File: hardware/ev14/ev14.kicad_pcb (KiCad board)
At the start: 4 copper layers, 75.2 x 80 mm, 173 parts, among them CN1 Conn_05x02_Female, J1 USB_C_Receptacle, J10 Conn_02x05_Counter_Clockwise, J2 Conn_01x02_Socket, J3 AudioJack4, J4 AudioJack4, J5 Conn_02x03_Odd_Even, J6 Conn_01x35_Socket, J7 Conn_02x05_Counter_Clockwise, J8 Conn_02x05_Counter_Clockwise, J9 Conn_02x05_Counter_Clockwise, Q1 2N7002, Q2 Q_Dual_NMOS_S1G1D2S2G2D1, Q3 PMOS, SW1 SW_SPDT, SW2 SW_Push, SW3 SW_Push, SW4 SW_Push, SW5 SW_Push, U1 BQ21040DBV, U10 STM32F405RGTx, U2 USBLC6-2P6, U3 STM32F072CBTx, U4 CH340C, U5 TPS63060, U6 WM8960CGEFL/RV, U7 ESP32-S3-WROOM-1, U8 M24C02-RMN6TP, U9 BM14B(0.8)-24DS-0.4V(53), Y1 Crystal_GND24

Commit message: First finished draft of Ev14
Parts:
- removed TP1, TP2, TP3, TP4: TestPoint, TestPoint:TestPoint_THTPad_D2.0mm_Drill1.0mm
- moved J10 3.19 mm to (233.2, 125.3)
- moved J7 3.19 mm to (246.8, 125.4)
- moved J8 3.19 mm to (233.2, 109.3)
- moved J9 3.19 mm to (246.9, 109.4)
- moved U2 1.95 mm to (197.9, 122.5), turned to 90 degrees
- moved C46 1.91 mm to (196.8, 119.1)
- moved R61 1.91 mm to (197.8, 119.1)
- moved R57 0.88 mm to (195.8, 119.2)
- moved SW3 0.08 mm to (176.5, 100.8)
- moved SW2 0.08 mm to (176.5, 109.6)
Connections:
- U10 pad 16: /UI_TX2_NET -> /UI_TX2_NET_N
- U10 pad 17: /UI_RX2_NET -> /UI_RX2_NET_P
- U7 pad 10: /UI_RX2_NET_- -> /UI_RX2_NET_P
- U7 pad 11: /UI_TX2_NET_+ -> /UI_TX2_NET_N
- U9 pad 23: /KB_LEDK_2&3 -> unconnected-(U9-Pad23)
- U9 pad 24: /KB_LEDA_3&4 -> unconnected-(U9-Pad24)
- U9 pad 25: /KB_LEDK_1&4 -> unconnected-(U9-Pad25)
- U9 pad 26: /KB_LEDA_1&2 -> unconnected-(U9-Pad26)
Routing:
- net +3.3V: track 134.3 -> 189.8 mm, vias 33 -> 41
- net GNDA: track 98.1 -> 152.5 mm, vias 7 -> 8
- net GND: track 232.4 -> 279.7 mm, vias 95 -> 109
- net /UI_TX2_NET: track 101.0 -> 126.9 mm, vias 2 -> 4
- net /UI_RX2_NET: track 101.0 -> 126.4 mm, vias 2 -> 4
- net /MGMT_NRST: track 97.5 -> 119.4 mm
- net /MGMT_BOOT: track 102.2 -> 122.4 mm
- net VBUS: track 27.1 -> 33.8 mm, vias 2 -> 4
- net /D_P: track 4.24 -> 10.5 mm
- net /D_N: track 6.08 -> 10.4 mm
- net /UI_SDA: track 141.3 -> 145.5 mm
- net /NET_TX1_MGMT: track 73.1 -> 77.1 mm
- net /UI_RTS1_MGMT: track 119.9 -> 123.6 mm
- net /USB_TX1_MGMT: track 54.7 -> 58.4 mm
- net /NET_RX1_MGMT: track 71.3 -> 74.7 mm
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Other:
- board size 75.2 x 80 mm -> 78.4 x 80 mm
- board text added: "EV14"
- board text added: "Finn Berg 2025/07/17"

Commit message: Updated complete EV14 draft
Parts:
- added J11: Conn_02x05_Counter_Clockwise, Hactar_Footprints:HDR-SMD_10P-P2.54-V-F-R2-C5-LS7.1-1, F.Cu at (245.7, 117.4)
- moved J7 12.2 mm to (258.9, 125.3)
- moved J9 12.0 mm to (258.9, 109.3)
- moved R65 0.41 mm to (215.1, 54.5)
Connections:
- U10 pad 16: /UI_TX2_NET_N -> /UI_TX2_NET
- U10 pad 17: /UI_RX2_NET_P -> /UI_RX2_NET
- U10 pad 20: /UI_LED_R -> /MIC_IO
- U10 pad 53: /MIC_IO -> /UI_LED_R
- U7 pad 10: /UI_RX2_NET_P -> /UI_RX2_NET
- U7 pad 11: /UI_TX2_NET_N -> /UI_TX2_NET
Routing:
- net GND: track 279.7 -> 342.6 mm, vias 109 -> 111
- net /UI_RX2_NET: track 126.4 -> 175.9 mm, vias 4 -> 5
- net /UI_TX2_NET: track 126.9 -> 175.4 mm, vias 4 -> 5
- net +3.3V: track 189.8 -> 221.3 mm, vias 41 -> 43
- net /NET_TX1_MGMT: track 77.1 -> 105.9 mm
- net /NET_RX1_MGMT: track 74.7 -> 102.4 mm
- net GNDA: track 152.5 -> 177.8 mm
- net /UI_RTS1_MGMT: track 123.6 -> 140.6 mm, vias 5 -> 3
- net Net-(J9-Pin_6): track 64.8 -> 81.7 mm
- net /MGMT_BOOT: track 122.4 -> 107.3 mm
- net Net-(J9-Pin_7): track 69.6 -> 84.6 mm
- net /MGMT_NRST: track 119.4 -> 104.7 mm
- net Net-(J9-Pin_8): track 72.9 -> 87.4 mm
- net /UI_CTS1_MGMT: track 119.6 -> 133.3 mm, vias 5 -> 3
- net /USB_RX1_MGMT: track 67.7 -> 81.0 mm
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- removed copper zone on B.Cu, net GNDA
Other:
- board size 78.4 x 80 mm -> 94.4 x 80 mm
- board text added: "+3.3V"
- board text added: "+3.3V -->"
- board text added: "BATTERY"
- board text added: "BOOT0"
- board text added: "DISPLAY"
- board text added: "FINN BERG 2025/07/22"
- board text added: "GND"
- board text added: "GND -->"
- board text added: "I2S_ADCDAT"
- board text added: "I2S_BCLK"
- board text added: "I2S_DACDAT"
- board text added: "I2S_DACLRC"
- board text added: "KEYBOARD"
- board text added: "LED_A"
- board text added: "LED_B"
- board text added: "LED_NET"
- board text added: "LED_UI"
- board text added: "MCLK"
- board text added: "MGMT_BOOT"
- board text added: "MGMT_CPU"
- board text added: "MGMT_DEBUG_1"
- board text added: "MGMT_DEBUG_2"
- board text added: "MGMT_NRST"
- board text added: "MGMT_SWCLK"
- board text added: "MGMT_SWDIO"
- board text added: "NET J-tag"
- board text added: "NET_BOOT"
- board text added: "NET_CPU"
- board text added: "NET_DEBUG_1"
- board text added: "NET_DEBUG_2"
- board text added: "NET_DEBUG_3"
- board text added: "NET_NRST"
- board text added: "NET_RX1_MGMT"
- board text added: "NET_TX1_MGMT"
- board text added: "NRST"
- board text added: "OSCILLATOR"
- board text added: "P2T"
- board text added: "P2T2AI"
- board text added: "Pin out: 1:3.3V 2:NET_MTMS 3:GND 4:NET_MTCK 5:GND 6:NET_MTDO 7:GND 8:NET_MTDI 9:GND 10:X"
- board text added: "SNAP HERE"
- board text added: "SWCLK"
- board text added: "SWDIO"
- board text added: "UI ST-Link"
- board text added: "UI_CPU"
- board text added: "UI_CTS1_MGMT"
- board text added: "UI_DEBUG_1"
- board text added: "UI_DEBUG_2"
- board text added: "UI_RTS1_MGMT"
- board text added: "UI_RX1_MGMT"
- board text added: "UI_RX2_NET"
- board text added: "UI_SCL"
- board text added: "UI_SDA"
- board text added: "UI_TX1_MGMT"
- board text added: "UI_TX2_NET"
- board text added: "USB_RX1_MGMT"
- board text added: "USB_TX1_MGMT"
- board text added: "VIN"
- board text added: "VOUT"
- board text added: "X"
- board text removed: "Finn Berg 2025/07/17"

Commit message: Final Version of EV14
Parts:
- removed J4: AudioJack4, Hactar_Footprints:AUDIO-SMD_PJ-242
- removed R37: 100k, Resistor_SMD:R_0402_1005Metric
- removed R63: 1k0, Resistor_SMD:R_0402_1005Metric
- added C49: 100n, Capacitor_SMD:C_0402_1005Metric, F.Cu at (191.7, 65.5)
- added CN2: PJ-242, Hactar_Footprints:AUDIO-SMD_PJ-242D-SMT, F.Cu at (189.3, 58.3)
- added R75: 4k7, Resistor_SMD:R_0402_1005Metric, F.Cu at (185.0, 55.6)
- J10: value Conn_02x05_Counter_Clockwise -> Conn_02x04_Odd_Even; footprint Hactar_Footprints:HDR-SMD_10P-P2.54-V-F-R2-C5-LS7.1-1 -> Hactar_Footprints:HDR-SMD_8P-P2.54-V-M-R2-C4-LS7.4
- moved J10 1.57 mm to (233.3, 126.8)
- moved Q3 0.32 mm to (182.6, 55.2)
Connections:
- net /UI_SCL renamed /UI_SCL1
- net /UI_SDA renamed /UI_SDA1
- J10 pad 2: /NET_TX1_MGMT -> /MGMT_SWCLK
- J10 pad 3: /NET_RX1_MGMT -> /NET_TX1_MGMT
- J10 pad 4: /NET_NRST -> /MGMT_SWDIO
- J10 pad 5: GND -> /NET_RX1_MGMT
- J10 pad 6: GND -> /MGMT_NRST
- J10 pad 7: /MGMT_BOOT -> /NET_NRST
- J10 pad 8: /MGMT_NRST -> /MGMT_BOOT
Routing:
- net +3.3V: track 221.3 -> 243.0 mm, vias 43 -> 44
- net Net-(Q2A-G): track 8.91 -> 22.2 mm, vias 0 -> 2
- net GND: track 342.6 -> 335.9 mm, vias 111 -> 110
- net /HP_R: track 25.1 -> 21.9 mm
- net GNDA: track 177.8 -> 180.4 mm, vias 8 -> 9
- net /NET_NRST: track 89.7 -> 92.0 mm
- net /MCLK: track 133.1 -> 131.4 mm
- net /MGMT_SWDIO: track 47.3 -> 45.9 mm
- net /UI_SCL1: track 144.1 -> 142.9 mm
- net /NET_TX1_MGMT: track 105.9 -> 107.0 mm
- net /NET_RX1_MGMT: track 102.4 -> 103.5 mm
- net /UI_RTS2_NET: track 52.2 -> 53.1 mm
- net /MGMT_NRST: track 104.7 -> 103.8 mm
- net Net-(Q2B-D): track 4.13 -> 3.27 mm
- net /UI_TX2_NET: track 175.4 -> 174.6 mm
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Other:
- outline, holes or cut-outs redrawn
- board text added: "BOARD"
- board text added: "CISCO"
- board text added: "DEV"

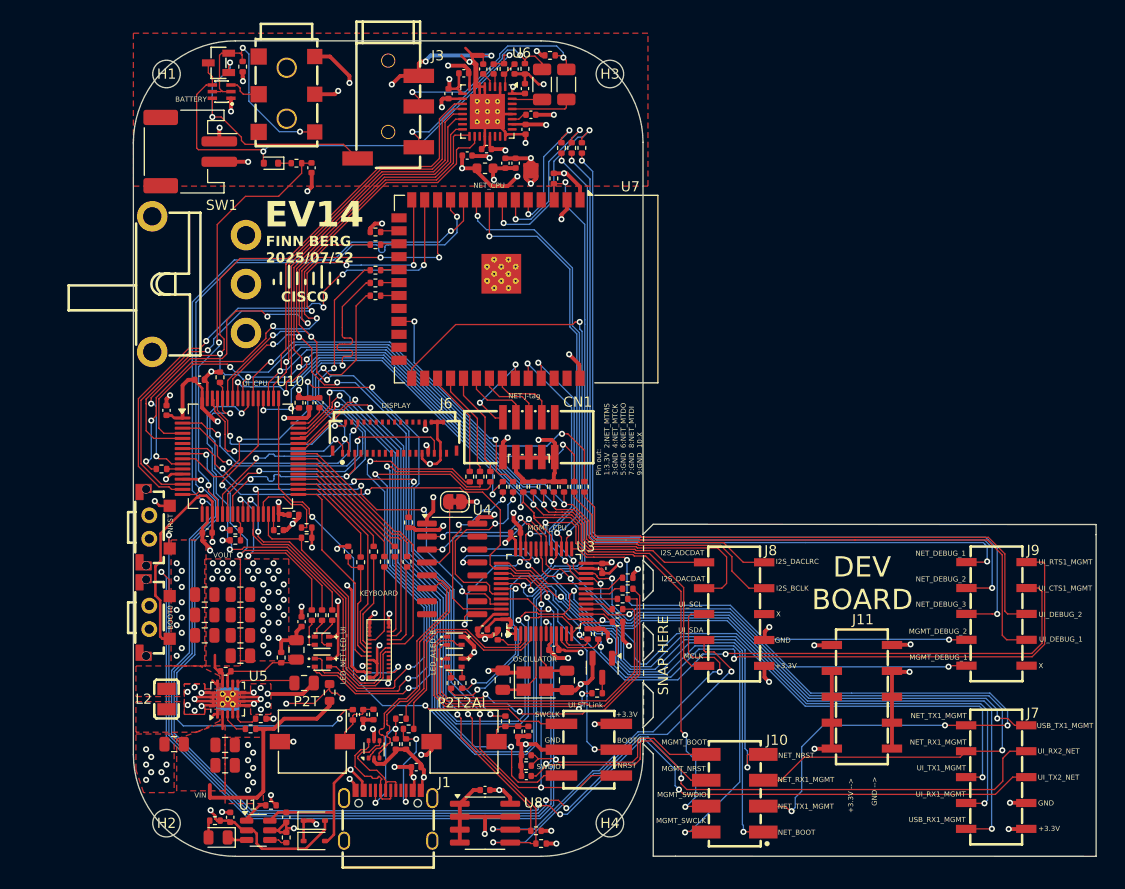
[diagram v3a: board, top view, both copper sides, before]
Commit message: chore: update headphone jacks to be 11.46mm apart. Fix issues that arose from that
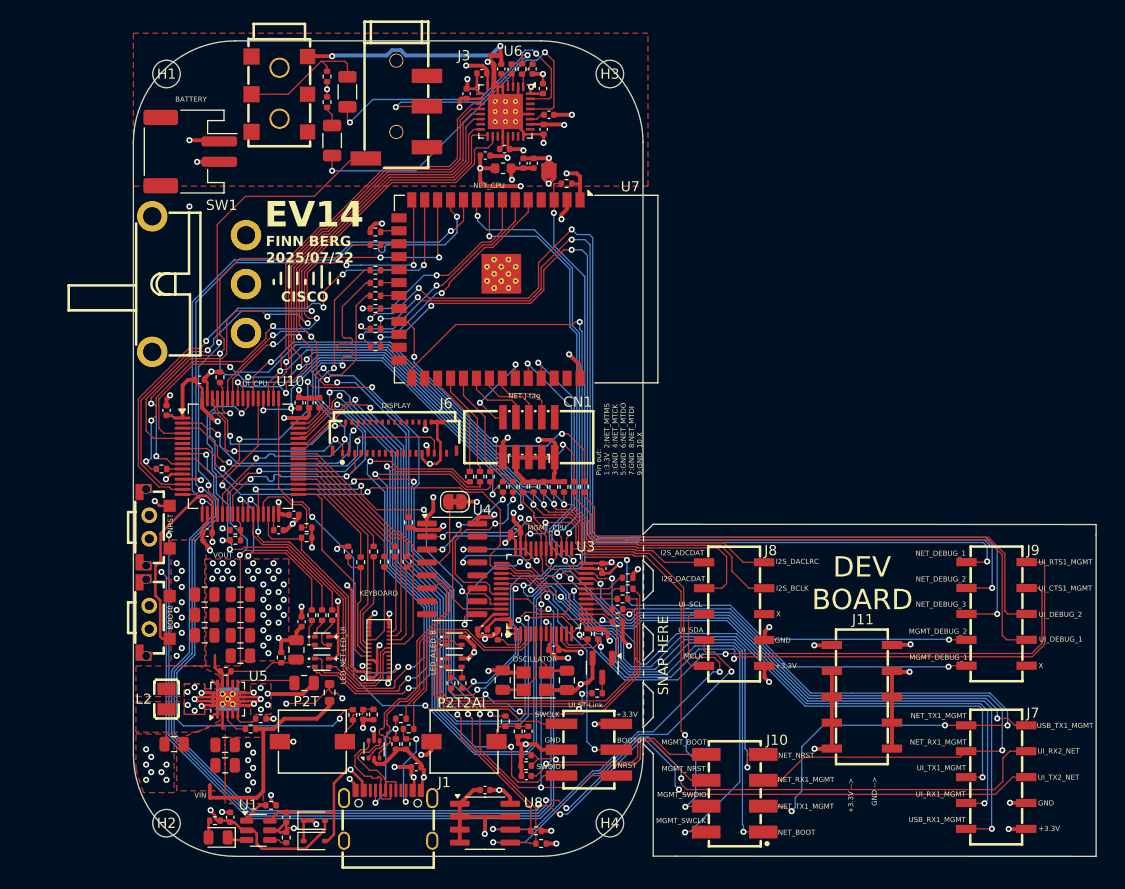
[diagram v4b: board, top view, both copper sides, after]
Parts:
- removed C49: 100n, Capacitor_SMD:C_0402_1005Metric
- removed D7: 1N4148WT, Diode_SMD:D_SOD-523
- removed Q2: Q_Dual_NMOS_S1G1D2S2G2D1, Hactar_Footprints:SOT-363_L2.1-W1.3-P0.65-LS2.3-BL
- removed Q3: PMOS, Hactar_Footprints:SOT-23-3_L2.9-W1.3-P1.90-LS2.4-BR
- removed R36: 47k, Resistor_SMD:R_0402_1005Metric
- removed R75: 4k7, Resistor_SMD:R_0402_1005Metric
- moved R70 26.7 mm to (198.0, 83.0), turned to 0 degrees
- moved R71 26.2 mm to (198.0, 81.3), turned to 0 degrees
- moved R72 25.7 mm to (198.0, 79.3), turned to 0 degrees
- moved C48 23.6 mm to (193.8, 62.8)
- moved R65 22.4 mm to (193.3, 59.0), turned to -90 degrees
- moved R32 19.4 mm to (193.3, 56.5)
- moved C34 19.1 mm to (195.3, 58.0)
- moved C10 1.77 mm to (212.5, 65.0)
- moved C11 1.77 mm to (213.5, 65.0)
- moved C28 1.77 mm to (210.7, 63.7)
- moved C33 1.77 mm to (215.0, 60.3)
- moved C36 1.77 mm to (211.4, 55.8)
- moved C37 1.77 mm to (213.4, 55.8)
- moved C7 1.77 mm to (208.8, 64.3)
- moved JP2 1.77 mm to (209.8, 54.5)
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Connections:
- CN2 pad 4: GNDA -> unconnected-(CN2-Pad4)
- CN2 pad 5: Net-(Q2A-G) -> unconnected-(CN2-Pad5)
- CN2 pad 6: Net-(Q2B-D) -> /HP_L
- J3 pad R1: /HP_R -> /MIC_P
- J3 pad R2: /MIC_N -> unconnected-(J3-PadR2)
- J3 pad S: Net-(Q2A-D) -> /MIC_IO
- J3 pad T: /HP_L -> unconnected-(J3-PadT)
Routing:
- net GNDA: track 180.4 -> 139.5 mm, vias 9 -> 7
- net Net-(U6-HP_R): track 6.16 -> 35.3 mm, vias 0 -> 2
- net /MIC_P: track 47.9 -> 19.7 mm
- net Net-(U6-HP_L): track 3.20 -> 30.4 mm, vias 0 -> 2
- net Net-(Q2A-D): track 25.1 -> 0.00 mm, vias 2 -> 0
- net Net-(Q2A-G): track 22.2 -> 0.00 mm, vias 2 -> 0
- net Net-(J9-Pin_8): track 87.4 -> 108.1 mm, vias 2 -> 4
- net /HP_R: track 21.9 -> 1.99 mm, vias 2 -> 0
- net Net-(J9-Pin_7): track 84.6 -> 101.3 mm, vias 2 -> 4
- net +3.3V: track 243.0 -> 226.7 mm, vias 44 -> 43
- net Net-(J9-Pin_6): track 81.7 -> 96.8 mm, vias 2 -> 4
- net /NET_DEBUG_1: track 13.0 -> 24.2 mm
- net GND: track 335.9 -> 326.6 mm
- net /HP_L: track 20.3 -> 13.1 mm, vias 2 -> 0
- net /NET_DEBUG_2: track 15.7 -> 22.7 mm
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
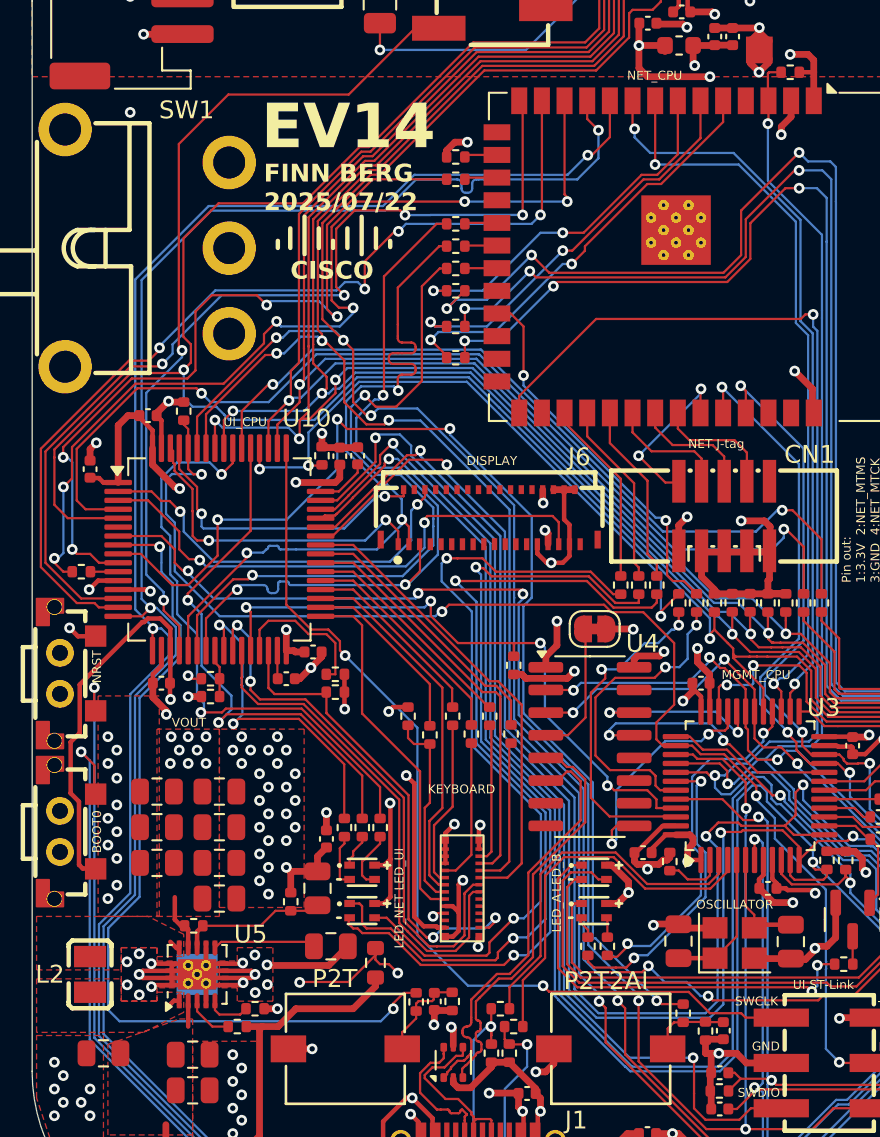
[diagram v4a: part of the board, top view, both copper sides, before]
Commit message: feat: cleaned up remaining pcb errors and warnings
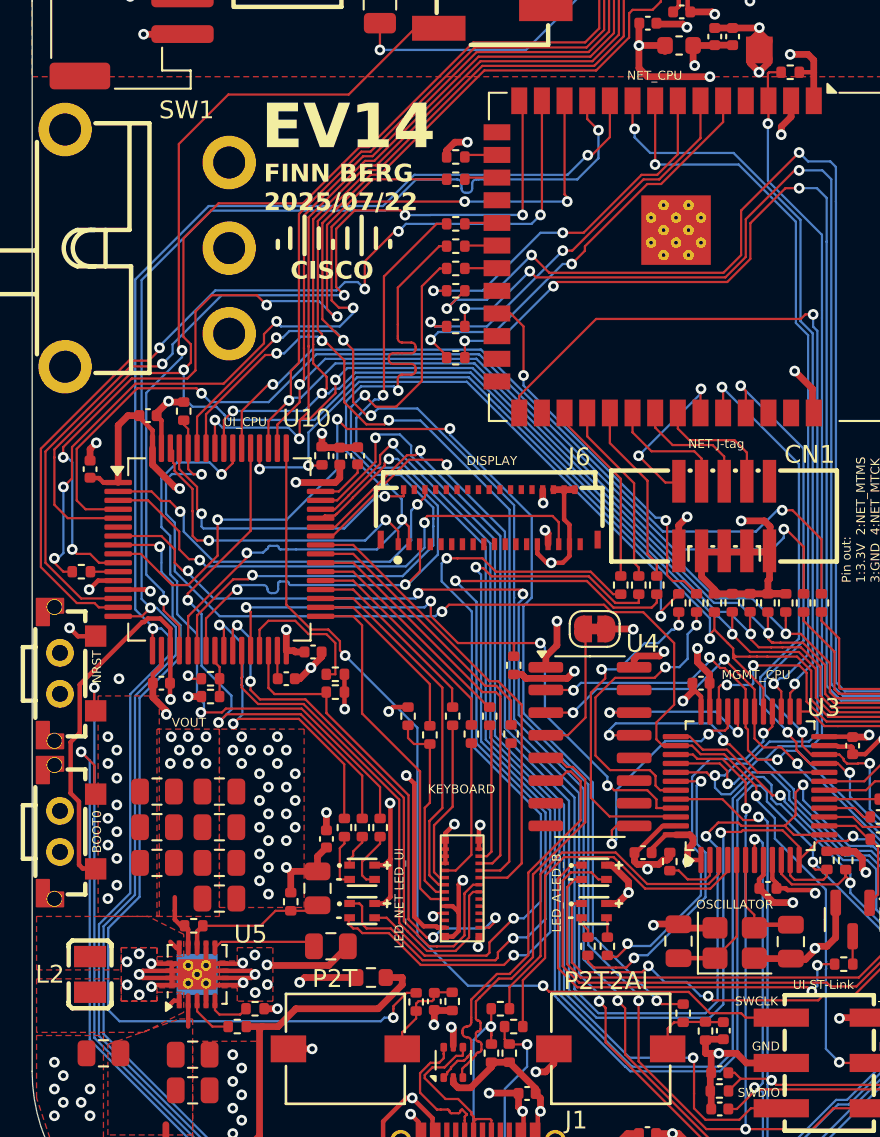
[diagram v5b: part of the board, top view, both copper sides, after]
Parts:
- moved R14 0.86 mm to (193.3, 117.8), turned to 0 degrees
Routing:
- net Net-(SW1-C): track 86.4 -> 61.0 mm
- net Net-(U5-VIN): track 22.8 -> 25.2 mm
- net GND: track 326.6 -> 326.4 mm, vias 110 -> 109
